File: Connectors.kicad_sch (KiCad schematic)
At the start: 21 parts, among them J10 Conn_01x08, J11 Conn_01x06, J12 Conn_01x06, J13 Conn_01x08, J14 Conn_01x02, J15 Conn_01x03, J16 Conn_01x03, J17 Conn_01x02, J18 USB4105-GF-A, J2 Conn_01x04, J20 Conn_02x07_Odd_Even, J3 Conn_01x04, J4 Conn_01x04, J5 Conn_01x04, J6 Conn_01x03, J7 Conn_01x04, J8 Conn_01x04, J9 Conn_01x04

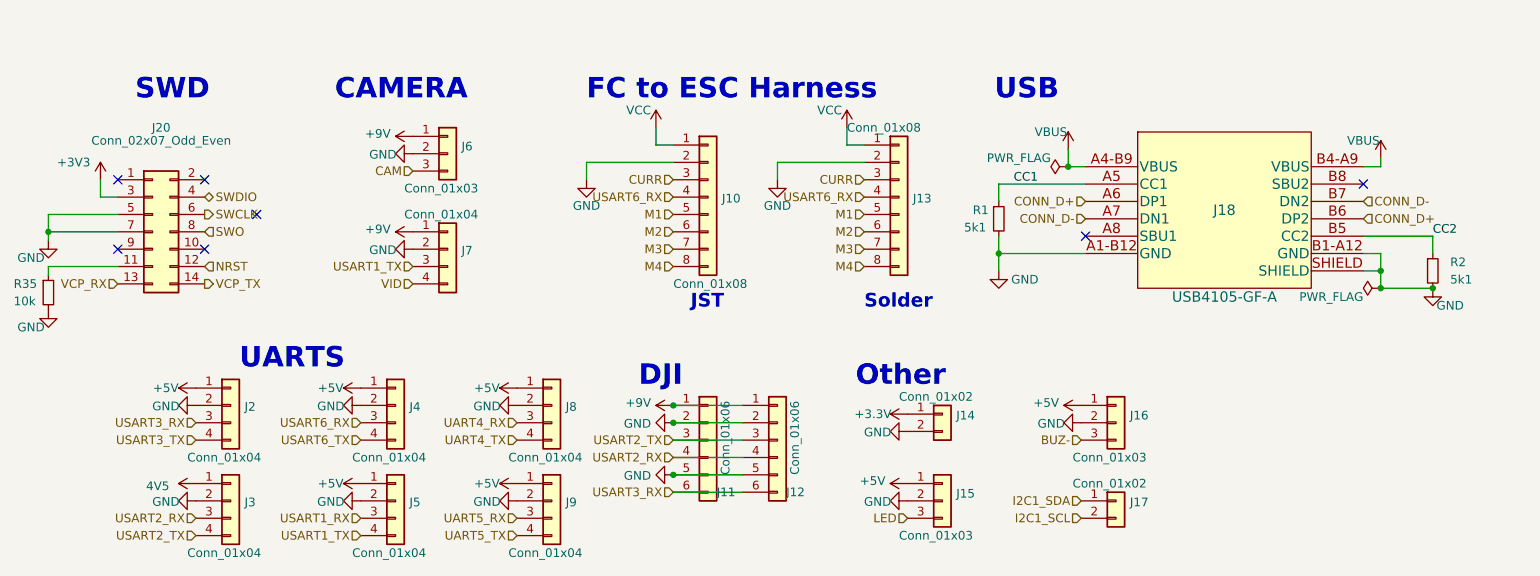
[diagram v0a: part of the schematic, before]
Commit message: Finished power and signal routing.
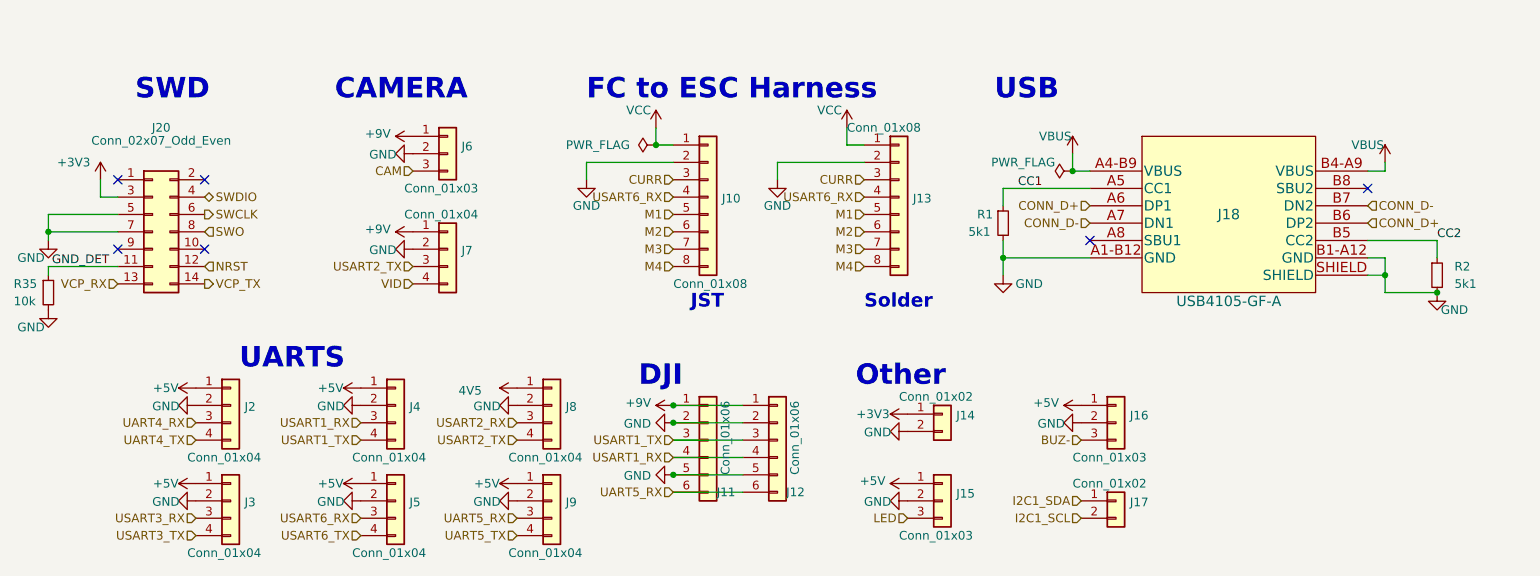
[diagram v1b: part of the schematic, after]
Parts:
- J12: footprint MyConnectors:Conn_DJI -> JPW_Connectors:Conn_DJI
- J13: footprint MyConnectors:Conn_8Edge -> JPW_Connectors:Conn_8Edge_SMT
- J14, J17: footprint MyConnectors:Conn_1x2 -> JPW_Connectors:Conn_1x2_SMT
- J15, J16, J6: footprint MyConnectors:Conn_1x3 -> JPW_Connectors:Conn_1x3_SMT
- J18: footprint MyConnectors:GCT_USB4105-GF-A -> JPW_Connectors:GCT_USB4105-GF-A
- J2, J3, J4, J5, J7, J8, J9: footprint MyConnectors:Conn_1x4 -> JPW_Connectors:Conn_1x4_SMT
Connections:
- net +3.3V is gone; now on net +3V3: J14.1 (Pin_1)
- net +5V: now also J3.1 (Pin_1); no longer J8.1 (Pin_1)
- net 4V5: now also J8.1 (Pin_1); no longer J3.1 (Pin_1)
- net UART4_RX: now also J2.3 (Pin_3); no longer J8.3 (Pin_3)
- net UART4_TX: now also J2.4 (Pin_4); no longer J8.4 (Pin_4)
- net UART5_RX: now also J11.6 (Pin_6), J12.6 (Pin_6)
- net USART1_RX: now also J11.4 (Pin_4), J12.4 (Pin_4), J4.3 (Pin_3); no longer J5.3 (Pin_3)
- net USART1_TX: now also J11.3 (Pin_3), J12.3 (Pin_3), J4.4 (Pin_4); no longer J5.4 (Pin_4), J7.3 (Pin_3)
- net USART2_RX: now also J8.3 (Pin_3); no longer J11.4 (Pin_4), J12.4 (Pin_4), J3.3 (Pin_3)
- net USART2_TX: now also J7.3 (Pin_3), J8.4 (Pin_4); no longer J11.3 (Pin_3), J12.3 (Pin_3), J3.4 (Pin_4)
- net USART3_RX: now also J3.3 (Pin_3); no longer J11.6 (Pin_6), J12.6 (Pin_6), J2.3 (Pin_3)
- net USART3_TX: now also J3.4 (Pin_4); no longer J2.4 (Pin_4)
- net USART6_RX: now also J5.3 (Pin_3); no longer J4.3 (Pin_3)
- net USART6_TX: now also J5.4 (Pin_4); no longer J4.4 (Pin_4)
- net GND_DET: now reaches J20.11 (Pin_11), R35.1
- no-connect marks 7 -> 6
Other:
- moved on the sheet: J18, R1, R2
